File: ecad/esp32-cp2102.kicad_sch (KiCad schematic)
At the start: 1 part, among them U3 ESP32-WROOM-32

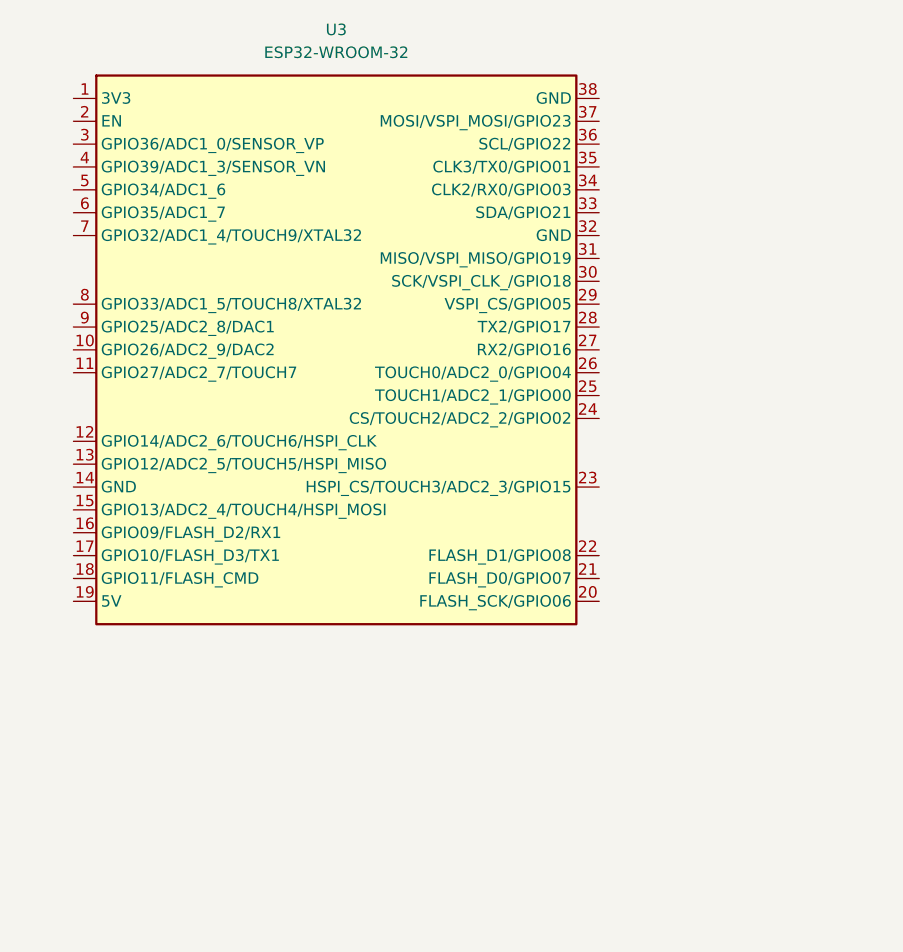
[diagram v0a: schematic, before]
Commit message: fead (ecad): update ESP32-CP2102 Schematic
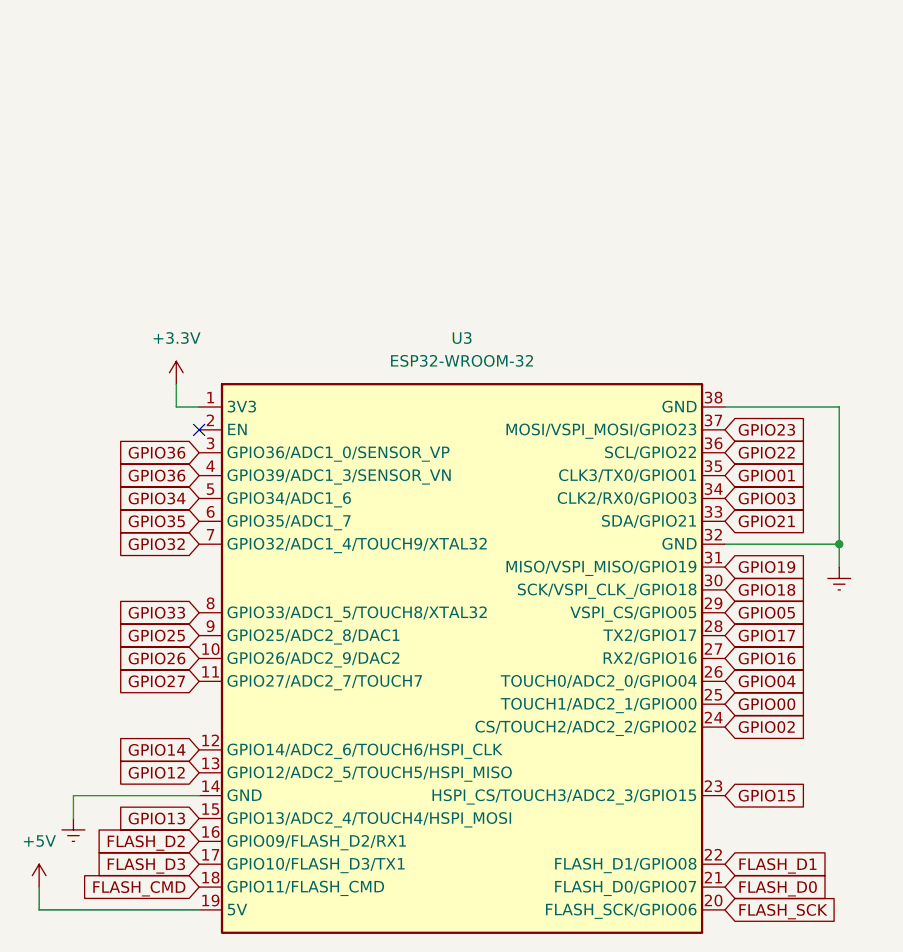
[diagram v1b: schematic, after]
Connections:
- net +3.3V: now reaches U3.1 (3V3)
- net GPIO26: now reaches U3.10 (GPIO26/ADC2_9/DAC2)
- net GPIO27: now reaches U3.11 (GPIO27/ADC2_7/TOUCH7)
- net GPIO14: now reaches U3.12 (GPIO14/ADC2_6/TOUCH6/HSPI_CLK)
- net GPIO12: now reaches U3.13 (GPIO12/ADC2_5/TOUCH5/HSPI_MISO)
- net Earth: now reaches U3.14 (GND)
- net Earth: now also U3.32 (GND), U3.38 (GND)
- net GPIO13: now reaches U3.15 (GPIO13/ADC2_4/TOUCH4/HSPI_MOSI)
- net FLASH_D2: now reaches U3.16 (GPIO09/FLASH_D2/RX1)
- net FLASH_D3: now reaches U3.17 (GPIO10/FLASH_D3/TX1)
- net FLASH_CMD: now reaches U3.18 (GPIO11/FLASH_CMD)
- net +5V: now reaches U3.19 (5V)
- net FLASH_SCK: now reaches U3.20 (FLASH_SCK/GPIO06)
- net FLASH_D0: now reaches U3.21 (FLASH_D0/GPIO07)
- net FLASH_D1: now reaches U3.22 (FLASH_D1/GPIO08)
- net GPIO15: now reaches U3.23 (HSPI_CS/TOUCH3/ADC2_3/GPIO15)
- net GPIO02: now reaches U3.24 (CS/TOUCH2/ADC2_2/GPIO02)
- net GPIO00: now reaches U3.25 (TOUCH1/ADC2_1/GPIO00)
- net GPIO04: now reaches U3.26 (TOUCH0/ADC2_0/GPIO04)
- net GPIO16: now reaches U3.27 (RX2/GPIO16)
- net GPIO17: now reaches U3.28 (TX2/GPIO17)
- net GPIO05: now reaches U3.29 (VSPI_CS/GPIO05)
- net GPIO36: now reaches U3.3 (GPIO36/ADC1_0/SENSOR_VP)
- net GPIO36: now also U3.4 (GPIO39/ADC1_3/SENSOR_VN)
- net GPIO18: now reaches U3.30 (SCK/VSPI_CLK_/GPIO18)
- net GPIO19: now reaches U3.31 (MISO/VSPI_MISO/GPIO19)
- net GPIO21: now reaches U3.33 (SDA/GPIO21)
- net GPIO03: now reaches U3.34 (CLK2/RX0/GPIO03)
- net GPIO01: now reaches U3.35 (CLK3/TX0/GPIO01)
- net GPIO22: now reaches U3.36 (SCL/GPIO22)
- net GPIO23: now reaches U3.37 (MOSI/VSPI_MOSI/GPIO23)
- net GPIO34: now reaches U3.5 (GPIO34/ADC1_6)
- net GPIO35: now reaches U3.6 (GPIO35/ADC1_7)
- net GPIO32: now reaches U3.7 (GPIO32/ADC1_4/TOUCH9/XTAL32)
- net GPIO33: now reaches U3.8 (GPIO33/ADC1_5/TOUCH8/XTAL32)
- net GPIO25: now reaches U3.9 (GPIO25/ADC2_8/DAC1)
- no-connect marks 0 -> 1
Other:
- title: (none) -> ESP32 AK Shield Schematik drawing CP2102
- moved on the sheet: U3

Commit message: feat (ecad): start PCB design
Left header pins and LEDs connected to devkits without ground-voltage
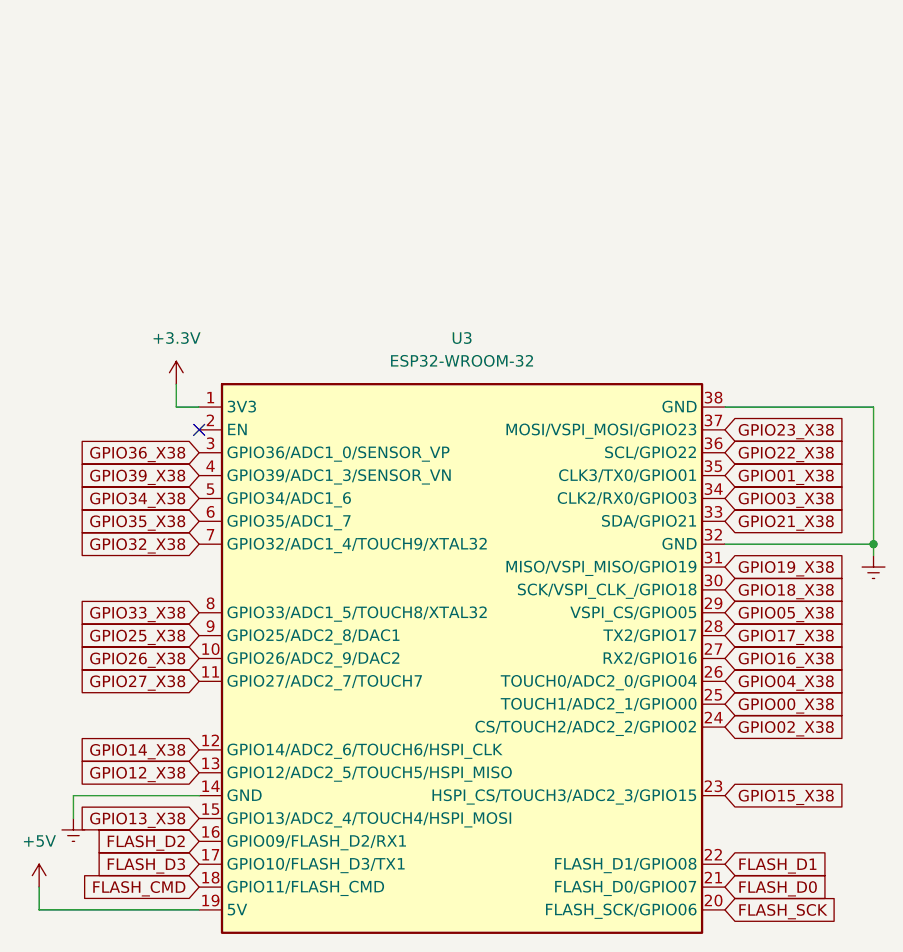
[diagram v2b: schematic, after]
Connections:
- net GPIO00 renamed GPIO00_X38
- net GPIO01 renamed GPIO01_X38
- net GPIO02 renamed GPIO02_X38
- net GPIO03 renamed GPIO03_X38
- net GPIO04 renamed GPIO04_X38
- net GPIO05 renamed GPIO05_X38
- net GPIO12 renamed GPIO12_X38
- net GPIO13 renamed GPIO13_X38
- net GPIO14 renamed GPIO14_X38
- net GPIO15 renamed GPIO15_X38
- net GPIO16 renamed GPIO16_X38
- net GPIO17 renamed GPIO17_X38
- net GPIO18 renamed GPIO18_X38
- net GPIO19 renamed GPIO19_X38
- net GPIO21 renamed GPIO21_X38
- net GPIO22 renamed GPIO22_X38
- net GPIO23 renamed GPIO23_X38
- net GPIO25 renamed GPIO25_X38
- net GPIO26 renamed GPIO26_X38
- net GPIO27 renamed GPIO27_X38
- net GPIO32 renamed GPIO32_X38
- net GPIO33 renamed GPIO33_X38
- net GPIO34 renamed GPIO34_X38
- net GPIO35 renamed GPIO35_X38
- net GPIO36 renamed GPIO36_X38
- net GPIO36_X38: no longer U3.4 (GPIO39/ADC1_3/SENSOR_VN)
- new net GPIO39_X38: U3.4 (GPIO39/ADC1_3/SENSOR_VN)
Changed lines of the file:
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@@
 	)
 	(junction
-		(at 118.11 72.39)
+		(at 121.92 72.39)
 		(diameter 0)
 		(color 0 0 0 0)
@@
 	(wire
 		(pts
-			(xy 118.11 57.15) (xy 118.11 72.39)
+			(xy 121.92 57.15) (xy 121.92 72.39)
 		)
 		(stroke
@@
 	(wire
 		(pts
-			(xy 118.11 72.39) (xy 105.41 72.39)
+			(xy 105.41 72.39) (xy 121.92 72.39)
 		)
 		(stroke
@@
 	(wire
 		(pts
-			(xy 118.11 74.93) (xy 118.11 72.39)
+			(xy 121.92 73.66) (xy 121.92 72.39)
 		)
 		(stroke
@@
 	(wire
 		(pts
-			(xy 105.41 57.15) (xy 118.11 57.15)
+			(xy 105.41 57.15) (xy 121.92 57.15)
 		)
 		(stroke
@@
 		)
 	)
-	(global_label "GPIO21"
+	(global_label "GPIO21_X38"
 		(shape input)
 		(at 105.41 69.85 0)
@@
 		)
 	)
-	(global_label "GPIO23"
+	(global_label "GPIO23_X38"
 		(shape input)
 		(at 105.41 59.69 0)
@@
 		)
 	)
-	(global_label "GPIO17"
+	(global_label "GPIO17_X38"
 		(shape input)
 		(at 105.41 82.55 0)
@@
 		)
 	)
-	(global_label "GPIO33"
+	(global_label "GPIO33_X38"
 		(shape input)
 		(at 46.99 80.01 180)
@@
 		)
 	)
-	(global_label "GPIO35"
+	(global_label "GPIO35_X38"
 		(shape input)
 		(at 46.99 69.85 180)
@@
 		)
 	)
-	(global_label "GPIO32"
+	(global_label "GPIO32_X38"
 		(shape input)
 		(at 46.99 72.39 180)
@@
 		)
 	)
-	(global_label "GPIO02"
+	(global_label "GPIO02_X38"
 		(shape input)
 		(at 105.41 92.71 0)
@@
 		)
 	)
-	(global_label "GPIO13"
+	(global_label "GPIO13_X38"
 		(shape input)
 		(at 46.99 102.87 180)
@@
 		)
 	)
-	(global_label "GPIO26"
+	(global_label "GPIO26_X38"
 		(shape input)
 		(at 46.99 85.09 180)
@@
 		)
 	)
-	(global_label "GPIO04"
+	(global_label "GPIO04_X38"
 		(shape input)
 		(at 105.41 87.63 0)
@@
 		)
 	)
-	(global_label "GPIO14"
+	(global_label "GPIO14_X38"
 		(shape input)
 		(at 46.99 95.25 180)
@@
 		)
 	)
-	(global_label "GPIO25"
+	(global_label "GPIO25_X38"
 		(shape input)
 		(at 46.99 82.55 180)
@@
 		)
 	)
-	(global_label "GPIO36"
+	(global_label "GPIO39_X38"
 		(shape input)
 		(at 46.99 64.77 180)
@@
 		)
 	)
-	(global_label "GPIO22"
+	(global_label "GPIO22_X38"
 		(shape input)
 		(at 105.41 62.23 0)
@@
 		)
 	)
-	(global_label "GPIO01"
+	(global_label "GPIO01_X38"
 		(shape input)
 		(at 105.41 64.77 0)
@@
 		)
 	)
-	(global_label "GPIO36"
+	(global_label "GPIO36_X38"
 		(shape input)
 		(at 46.99 62.23 180)
@@
 		)
 	)
-	(global_label "GPIO00"
+	(global_label "GPIO00_X38"
 		(shape input)
 		(at 105.41 90.17 0)
@@
 		)
 	)
-	(global_label "GPIO34"
+	(global_label "GPIO34_X38"
 		(shape input)
 		(at 46.99 67.31 180)
@@
 		)
 	)
-	(global_label "GPIO03"
+	(global_label "GPIO03_X38"
 		(shape input)
 		(at 105.41 67.31 0)
@@
 		)
 	)
-	(global_label "GPIO15"
+	(global_label "GPIO15_X38"
 		(shape input)
 		(at 105.41 100.33 0)
@@
 		)
 	)
-	(global_label "GPIO19"
+	(global_label "GPIO19_X38"
 		(shape input)
 		(at 105.41 74.93 0)
@@
 		)
 	)
-	(global_label "GPIO16"
+	(global_label "GPIO16_X38"
 		(shape input)
 		(at 105.41 85.09 0)
@@
 		)
 	)
-	(global_label "GPIO27"
+	(global_label "GPIO27_X38"
 		(shape input)
 		(at 46.99 87.63 180)
@@
 		)
 	)
-	(global_label "GPIO05"
+	(global_label "GPIO05_X38"
 		(shape input)
 		(at 105.41 80.01 0)
@@
 		)
 	)
-	(global_label "GPIO18"
+	(global_label "GPIO18_X38"
 		(shape input)
 		(at 105.41 77.47 0)
@@
 		)
 	)
-	(global_label "GPIO12"
+	(global_label "GPIO12_X38"
 		(shape input)
 		(at 46.99 97.79 180)
@@
 	(symbol
 		(lib_id "power:Earth")
-		(at 118.11 74.93 0)
+		(at 121.92 73.66 0)
 		(unit 1)
 		(exclude_from_sim no)
@@
 		(fields_autoplaced yes)
 		(property "Reference" "#PWR016"
-			(at 118.11 81.28 0)
+			(at 121.92 80.01 0)
 			(effects
 				(font
@@
 		)
 		(property "Value" "Earth"
-			(at 118.11 80.01 0)
+			(at 121.92 78.74 0)
 			(effects
 				(font
@@
 		)
 		(property "Footprint" ""
-			(at 118.11 74.93 0)
+			(at 121.92 73.66 0)
 			(effects
 				(font
@@
 		)
 		(property "Datasheet" "~"
-			(at 118.11 74.93 0)
+			(at 121.92 73.66 0)
 			(effects
 				(font
@@
 		)
 		(property "Description" "Power symbol creates a global label with name \"Earth\""
-			(at 118.11 74.93 0)
-			(effects
-				(font
+			(at 121.92 73.66 0)
+			(effects
+				(font
